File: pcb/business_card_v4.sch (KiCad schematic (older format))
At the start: 67 parts, among them J1 Conn_01x05_Male, J2 Conn_01x01_Male, SW1 SW_SPST, U1 MIC5504-3.3YM5, U2 STM32G030F6P6

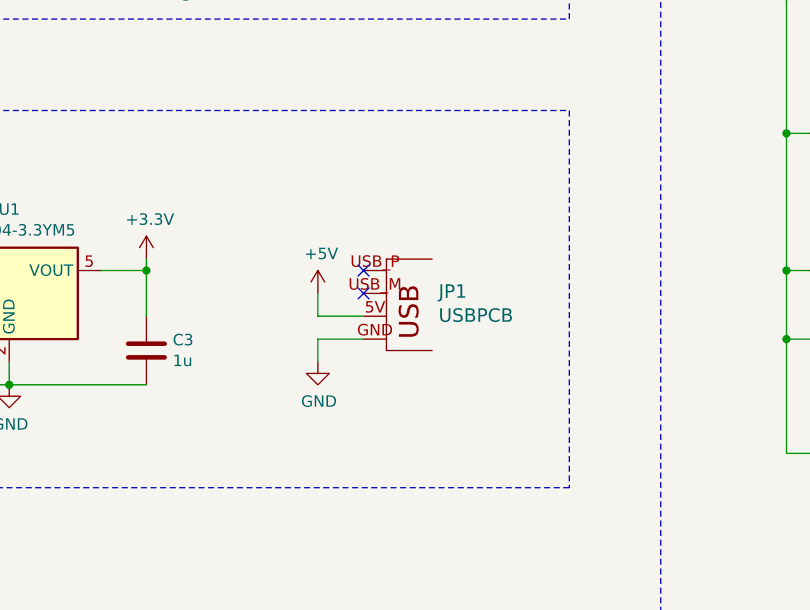
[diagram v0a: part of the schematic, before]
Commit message: create a net and update version of file names
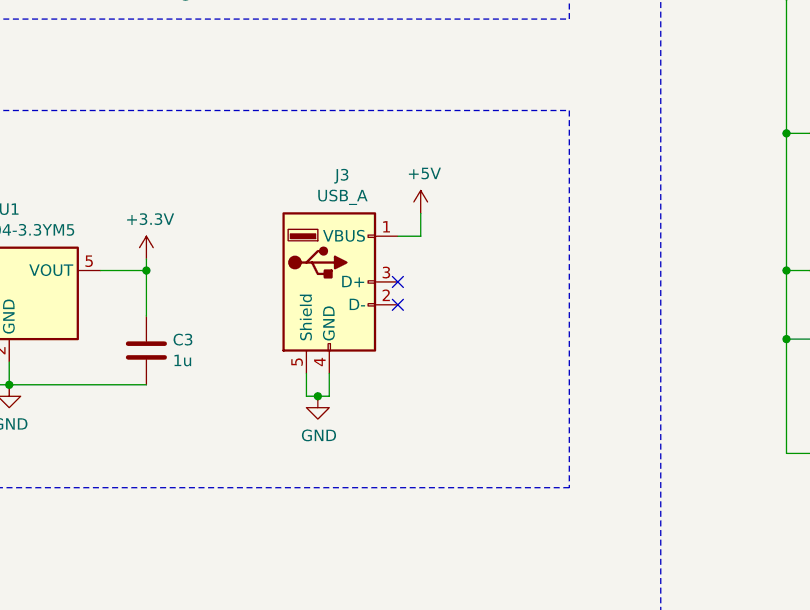
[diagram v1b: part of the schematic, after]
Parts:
- removed JP1: USBPCB, business_card_v1:USB-A-PCB, symbol business_card_v1-eagle-import:USBPCB
- added J3: USB_A, Kevin-Lutzer-Kicad-Lbr:USB-A-PCB, symbol Connector:USB_A
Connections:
- net +5V: now also J3.1 (VBUS)
- net GND: now also J3.4 (GND), J3.5 (Shield)
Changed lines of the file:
@@
 Text GLabel 1200 3200 2    50   Input ~ 0
 RST
-$Comp
-L power:GND #PWR0112
-U 1 1 5ED9E13B
-P 2800 5350
-F 0 "#PWR0112" H 2800 5100 50  0001 C CNN
-F 1 "GND" H 2805 5177 50  0000 C CNN
-F 2 "" H 2800 5350 50  0001 C CNN
-F 3 "" H 2800 5350 50  0001 C CNN
-	1    2800 5350
-	1    0    0    -1
-$EndComp
-Wire Wire Line
-	2800 5150 3000 5150
-Wire Wire Line
-	2800 5250 3000 5250
-Wire Wire Line
-	2800 5050 2800 5150
-Wire Wire Line
-	2800 5250 2800 5350
-$Comp
-L power:+5V #PWR0111
-U 1 1 5EE81479
-P 2800 5050
-F 0 "#PWR0111" H 2800 4900 50  0001 C CNN
-F 1 "+5V" H 2815 5223 50  0000 C CNN
-F 2 "" H 2800 5050 50  0001 C CNN
-F 3 "" H 2800 5050 50  0001 C CNN
-	1    2800 5050
-	1    0    0    -1
-$EndComp
 Wire Wire Line
 	1050 5150 850  5150
@@
 NoConn ~ 2050 2400
 NoConn ~ 2050 2300
-NoConn ~ 3000 5050
-NoConn ~ 3000 4950
-$Comp
-L business_card_v1-eagle-import:USBPCB JP1
-U 1 1 5EB91CEE
-P 3100 5250
-F 0 "JP1" H 3328 5458 59  0000 L CNN
-F 1 "USBPCB" H 3328 5353 59  0000 L CNN
-F 2 "business_card_v1:USB-A-PCB" H 3100 5250 50  0001 C CNN
-F 3 "" H 3100 5250 50  0001 C CNN
-	1    3100 5250
-	1    0    0    -1
-$EndComp
 $Comp
 L MCU_ST_STM32G0:STM32G030F6P6 U2
@@
 Wire Wire Line
 	1750 2100 1850 2100
+$Comp
+L Connector:USB_A J3
+U 1 1 5F2F7A93
+P 2850 5000
+F 0 "J3" H 2907 5467 50  0000 C CNN
+F 1 "USB_A" H 2907 5376 50  0000 C CNN
+F 2 "Kevin-Lutzer-Kicad-Lbr:USB-A-PCB" H 3000 4950 50  0001 C CNN
+F 3 " ~" H 3000 4950 50  0001 C CNN
+	1    2850 5000
+	1    0    0    -1
+$EndComp
+$Comp
+L power:+5V #PWR0114
+U 1 1 5F2FC9FB
+P 3250 4700
+F 0 "#PWR0114" H 3250 4550 50  0001 C CNN
+F 1 "+5V" H 3265 4873 50  0000 C CNN
+F 2 "" H 3250 4700 50  0001 C CNN
+F 3 "" H 3250 4700 50  0001 C CNN
+	1    3250 4700
+	1    0    0    -1
+$EndComp
+$Comp
+L power:GND #PWR0115
+U 1 1 5F2FD3B2
+P 2800 5500
+F 0 "#PWR0115" H 2800 5250 50  0001 C CNN
+F 1 "GND" H 2805 5327 50  0000 C CNN
+F 2 "" H 2800 5500 50  0001 C CNN
+F 3 "" H 2800 5500 50  0001 C CNN
+	1    2800 5500
+	1    0    0    -1
+$EndComp
+Wire Wire Line
+	2750 5400 2750 5500
+Wire Wire Line
+	2750 5500 2800 5500
+Wire Wire Line
+	2850 5500 2850 5400
+Connection ~ 2800 5500
+Wire Wire Line
+	2800 5500 2850 5500
+Wire Wire Line
+	3150 4800 3250 4800
+Wire Wire Line
+	3250 4800 3250 4700
+NoConn ~ 3150 5000
+NoConn ~ 3150 5100
 $EndSCHEMATC

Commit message: update
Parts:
- added JP1: USBPCB, business_card_v1:USB-A-PCB, symbol business_card_v1-eagle-import:USBPCB
- renumbered J3 to J?
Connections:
- net +5V: now also JP1.5V (VBUS)
- net GND: now also JP1.GND
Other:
- moved on the sheet: J?
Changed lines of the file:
@@
 Text GLabel 1200 3200 2    50   Input ~ 0
 RST
+$Comp
+L power:GND #PWR0112
+U 1 1 5ED9E13B
+P 2800 5350
+F 0 "#PWR0112" H 2800 5100 50  0001 C CNN
+F 1 "GND" H 2805 5177 50  0000 C CNN
+F 2 "" H 2800 5350 50  0001 C CNN
+F 3 "" H 2800 5350 50  0001 C CNN
+	1    2800 5350
+	1    0    0    -1
+$EndComp
+Wire Wire Line
+	2800 5150 3000 5150
+Wire Wire Line
+	2800 5250 3000 5250
+Wire Wire Line
+	2800 5050 2800 5150
+Wire Wire Line
+	2800 5250 2800 5350
+$Comp
+L power:+5V #PWR0111
+U 1 1 5EE81479
+P 2800 5050
+F 0 "#PWR0111" H 2800 4900 50  0001 C CNN
+F 1 "+5V" H 2815 5223 50  0000 C CNN
+F 2 "" H 2800 5050 50  0001 C CNN
+F 3 "" H 2800 5050 50  0001 C CNN
+	1    2800 5050
+	1    0    0    -1
+$EndComp
 Wire Wire Line
 	1050 5150 850  5150
@@
 NoConn ~ 2050 2400
 NoConn ~ 2050 2300
+NoConn ~ 3000 5050
+NoConn ~ 3000 4950
+$Comp
+L business_card_v1-eagle-import:USBPCB JP1
+U 1 1 5EB91CEE
+P 3100 5250
+F 0 "JP1" H 3328 5458 59  0000 L CNN
+F 1 "USBPCB" H 3328 5353 59  0000 L CNN
+F 2 "business_card_v1:USB-A-PCB" H 3100 5250 50  0001 C CNN
+F 3 "" H 3100 5250 50  0001 C CNN
+	1    3100 5250
+	1    0    0    -1
+$EndComp
 $Comp
 L MCU_ST_STM32G0:STM32G030F6P6 U2
@@
 	1750 2100 1850 2100
 $Comp
-L Connector:USB_A J3
+L Connector:USB_A J?
 U 1 1 5F2F7A93
-P 2850 5000
-F 0 "J3" H 2907 5467 50  0000 C CNN
-F 1 "USB_A" H 2907 5376 50  0000 C CNN
-F 2 "Kevin-Lutzer-Kicad-Lbr:USB-A-PCB" H 3000 4950 50  0001 C CNN
-F 3 " ~" H 3000 4950 50  0001 C CNN
-	1    2850 5000
+P 1750 6650
+F 0 "J?" H 1807 7117 50  0000 C CNN
+F 1 "USB_A" H 1807 7026 50  0000 C CNN
+F 2 "Kevin-Lutzer-Kicad-Lbr:USB-A-PCB" H 1900 6600 50  0001 C CNN
+F 3 " ~" H 1900 6600 50  0001 C CNN
+	1    1750 6650
 	1    0    0    -1
 $EndComp
 $Comp
-L power:+5V #PWR0114
+L power:+5V #PWR?
 U 1 1 5F2FC9FB
-P 3250 4700
-F 0 "#PWR0114" H 3250 4550 50  0001 C CNN
-F 1 "+5V" H 3265 4873 50  0000 C CNN
-F 2 "" H 3250 4700 50  0001 C CNN
-F 3 "" H 3250 4700 50  0001 C CNN
-	1    3250 4700
+P 2150 6350
+F 0 "#PWR?" H 2150 6200 50  0001 C CNN
+F 1 "+5V" H 2165 6523 50  0000 C CNN
+F 2 "" H 2150 6350 50  0001 C CNN
+F 3 "" H 2150 6350 50  0001 C CNN
+	1    2150 6350
 	1    0    0    -1
 $EndComp
 $Comp
-L power:GND #PWR0115
+L power:GND #PWR?
 U 1 1 5F2FD3B2
-P 2800 5500
-F 0 "#PWR0115" H 2800 5250 50  0001 C CNN
-F 1 "GND" H 2805 5327 50  0000 C CNN
-F 2 "" H 2800 5500 50  0001 C CNN
-F 3 "" H 2800 5500 50  0001 C CNN
-	1    2800 5500
+P 1700 7150
+F 0 "#PWR?" H 1700 6900 50  0001 C CNN
+F 1 "GND" H 1705 6977 50  0000 C CNN
+F 2 "" H 1700 7150 50  0001 C CNN
+F 3 "" H 1700 7150 50  0001 C CNN
+	1    1700 7150
 	1    0    0    -1
 $EndComp
 Wire Wire Line
-	2750 5400 2750 5500
-Wire Wire Line
-	2750 5500 2800 5500
-Wire Wire Line
-	2850 5500 2850 5400
-Connection ~ 2800 5500
-Wire Wire Line
-	2800 5500 2850 5500
-Wire Wire Line
-	3150 4800 3250 4800
-Wire Wire Line
-	3250 4800 3250 4700
-NoConn ~ 3150 5000
-NoConn ~ 3150 5100
+	1650 7050 1650 7150
+Wire Wire Line
+	1650 7150 1700 7150
+Wire Wire Line
+	1750 7150 1750 7050
+Connection ~ 1700 7150
+Wire Wire Line
+	1700 7150 1750 7150
+Wire Wire Line
+	2050 6450 2150 6450
+Wire Wire Line
+	2150 6450 2150 6350
 $EndSCHEMATC
